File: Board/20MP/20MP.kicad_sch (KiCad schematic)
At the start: 93 parts

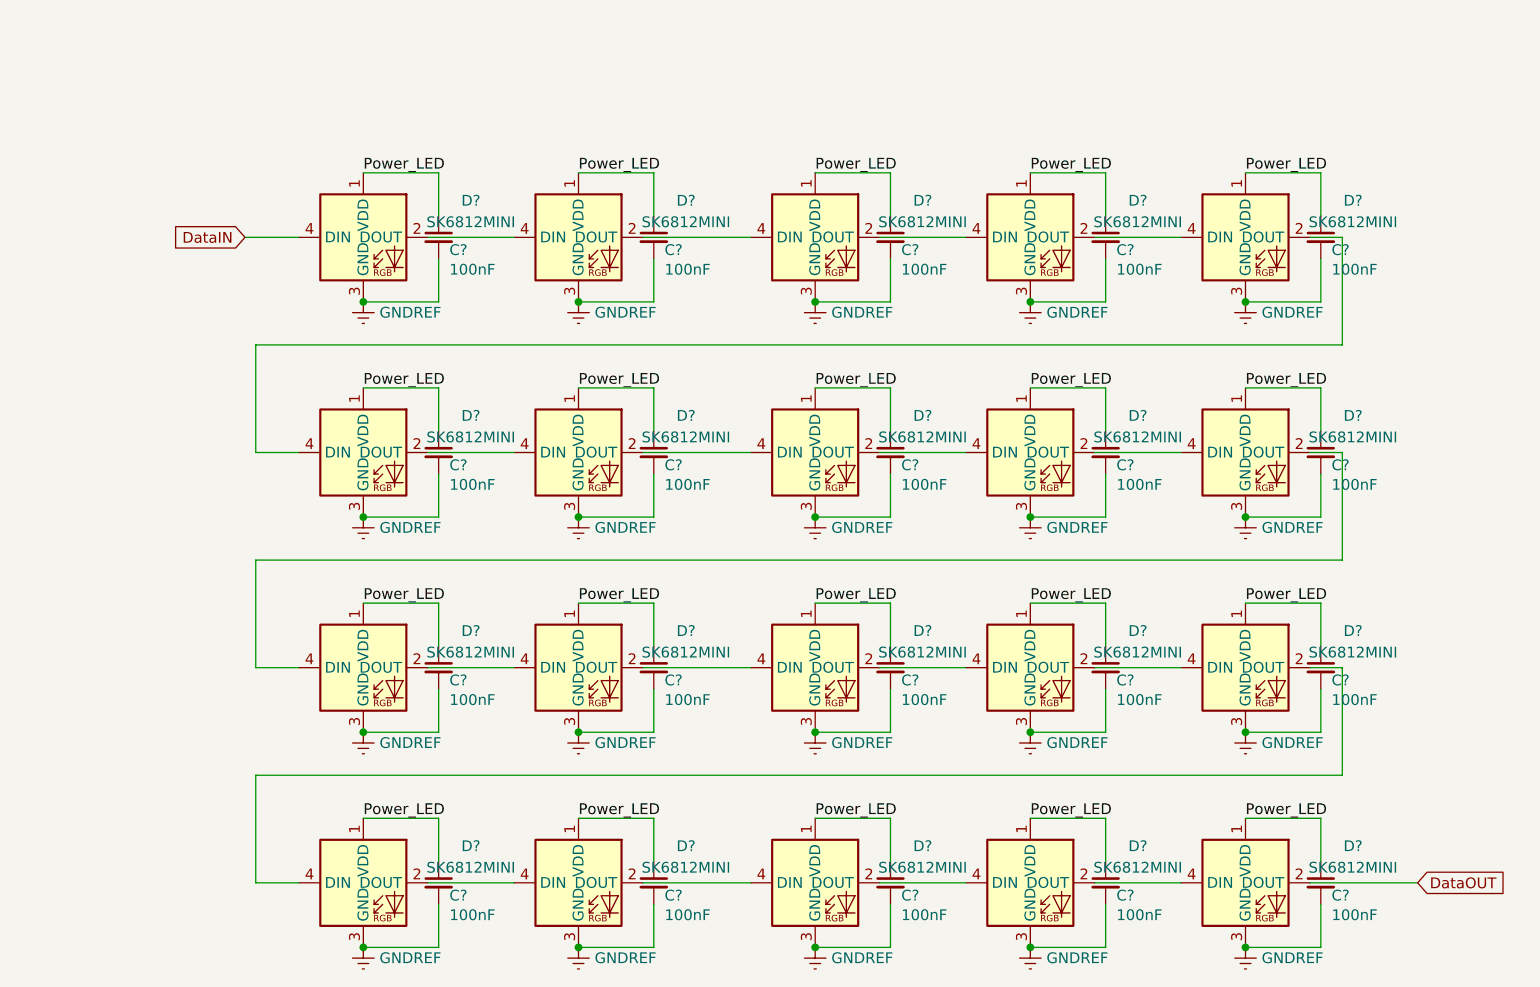
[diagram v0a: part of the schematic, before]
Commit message: removed led's
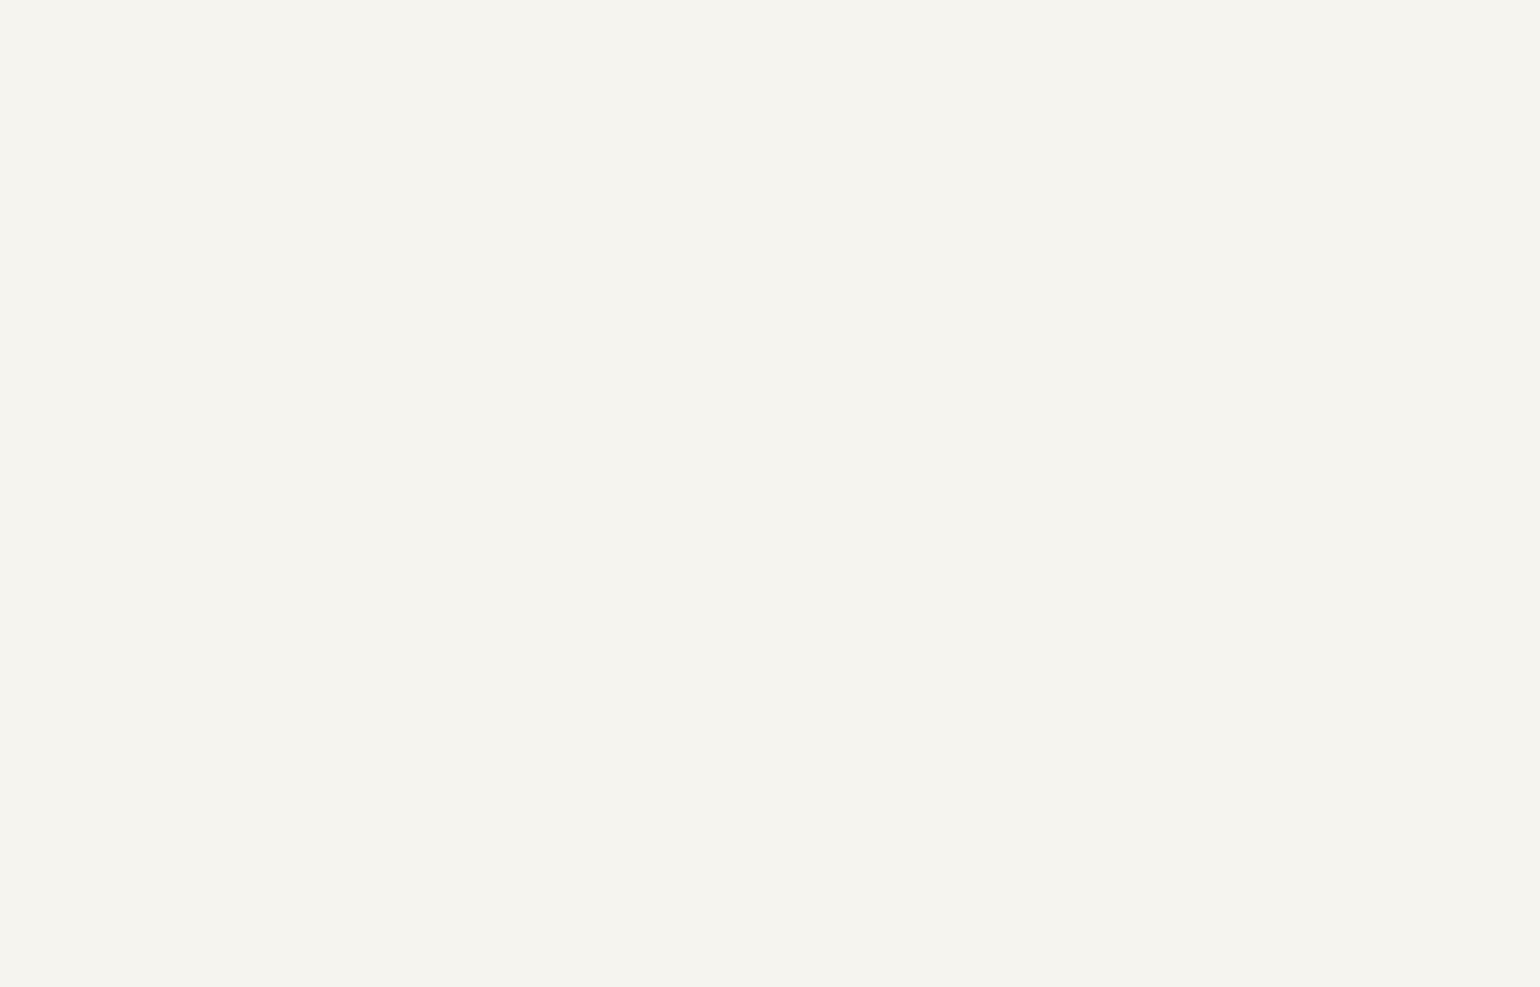
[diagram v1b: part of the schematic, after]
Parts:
- removed C? (x20): 100nF, led:led_capacitor, symbol Device:C_Small
- removed D? (x20): SK6812MINI, led:SK6812MINI_3.5x3.7mm_SMD-Flipped-Back, symbol randomSymbols:SK6812MINI-E

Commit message: removed LED's and added first librarys
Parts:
- removed D? (x22): 1.25V@150mA, led:D_SOD-123, symbol led:D_Small
- added J1: Conn_01x02_Male, Connector_JST:JST_EH_S2B-EH_1x02_P2.50mm_Horizontal, symbol Connector:Conn_01x02_Male
- added SW1: SHOU_HAN_MSK12C02-HB, led:SHOU HAN MSK12C02-HB, symbol randomSymbols:SHOU_HAN_MSK12C02-HB
- added U1: nice_nano, nice-nano-all-pins:nice_nano, symbol nice_nano:nice_nano
- MX1, MX10, MX11, MX12, MX13, MX14, MX15, MX16, MX17, MX18, MX19, MX2, MX20, MX3, MX4, MX5, MX6, MX7, MX8, MX9: renamed from MX?; footprint kailh-switches-hotswap:Kailh-Hotswap-1U -> mx-switches:CherryMX-1.00U
- gave numbers to parts that had none: 11
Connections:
- net COL0: now also U1.19 (AIN5/P0.29)
- net COL1: now also U1.18 (AIN0/P0.02)
- net COL2: now also U1.17 (P1.15)
- net COL3: now also U1.16 (P1.13)
- net COL4: now also U1.15 (P1.11)
- net COL5: now also U1.14 (NFC2/P0.10)
- net GND: now also SW1.4 (GND), U1.23 (GND), U1.3 (GND), U1.4 (GND)
- net ROW0: now also MX1.2 (ROW), MX13.2 (ROW), MX17.2 (ROW), MX5.2 (ROW), MX9.2 (ROW), SW2.S1, U1.1 (TX0/P0.06)
- net ROW1: now also MX10.2 (ROW), MX14.2 (ROW), MX18.2 (ROW), MX2.2 (ROW), MX6.2 (ROW), SW3.S1, U1.2 (RX1/P0.08)
- net ROW2: now also MX11.2 (ROW), MX15.2 (ROW), MX19.2 (ROW), MX3.2 (ROW), MX7.2 (ROW), U1.5 (P0.17)
- net ROW3: now also MX12.2 (ROW), MX16.2 (ROW), MX20.2 (ROW), MX4.2 (ROW), MX8.2 (ROW), U1.6 (P0.20)
- new net: J1.2 (Pin_2), SW1.3
- new net B+: SW1.2, U1.34 (BATIN/P0.04)
- new net B-: J1.1 (Pin_1), U1.30 (GND)
- new net VCC: U1.21 (VCC)
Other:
- moved on the sheet: MX1, MX10, MX11, MX12, MX13, MX14, MX15, MX16, MX17, MX18, MX19, MX2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

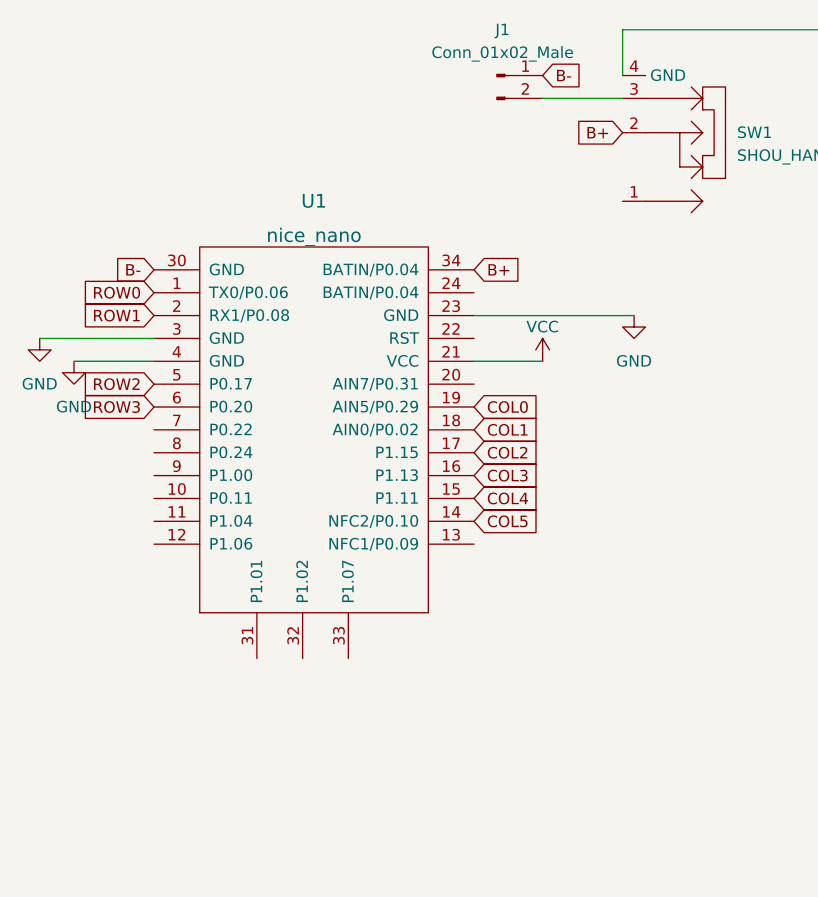
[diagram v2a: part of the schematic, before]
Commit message: added nice_nanoV2
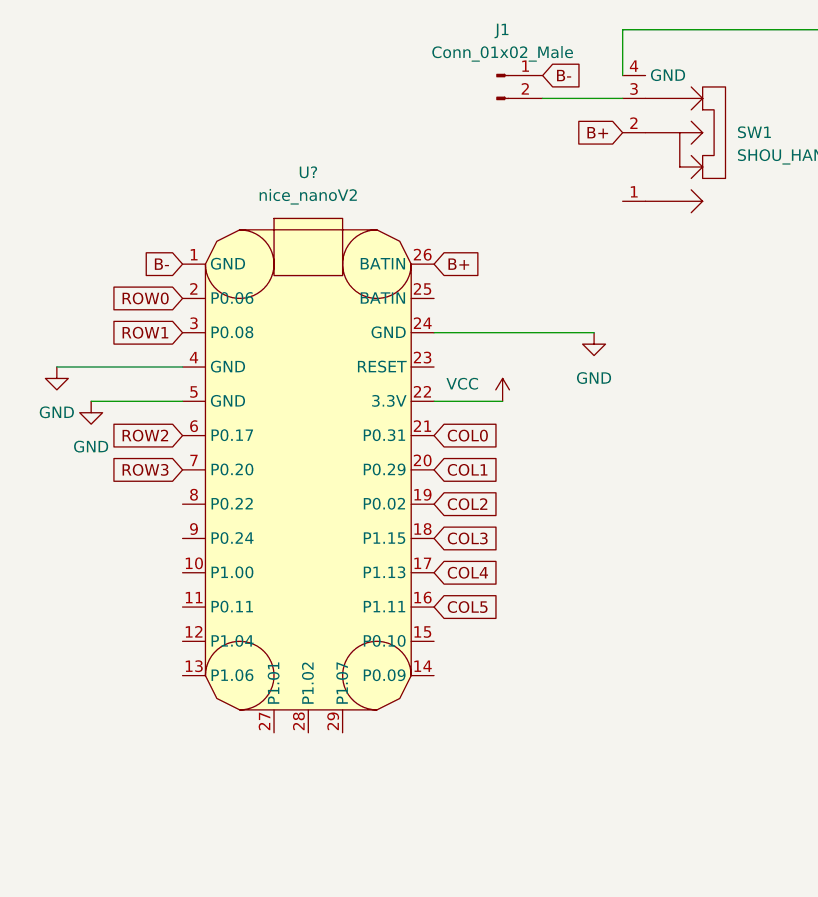
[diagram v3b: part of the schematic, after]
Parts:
- removed U1: nice_nano, nice-nano-all-pins:nice_nano, symbol nice_nano:nice_nano
- added U?: nice_nanoV2, symbol microcontroller:nice_nanoV2
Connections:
- net B+: now also U?.26 (BATIN)
- net B-: now also U?.1 (GND)
- net COL0: now also U?.21 (P0.31)
- net COL1: now also U?.20 (P0.29)
- net COL2: now also U?.19 (P0.02)
- net COL3: now also U?.18 (P1.15)
- net COL4: now also U?.17 (P1.13)
- net COL5: now also U?.16 (P1.11)
- net GND: now also U?.24 (GND), U?.4 (GND), U?.5 (GND)
- net ROW0: now also U?.2 (P0.06)
- net ROW1: now also U?.3 (P0.08)
- net ROW2: now also U?.6 (P0.17)
- net ROW3: now also U?.7 (P0.20)
- net VCC: now also U?.22 (3.3V)

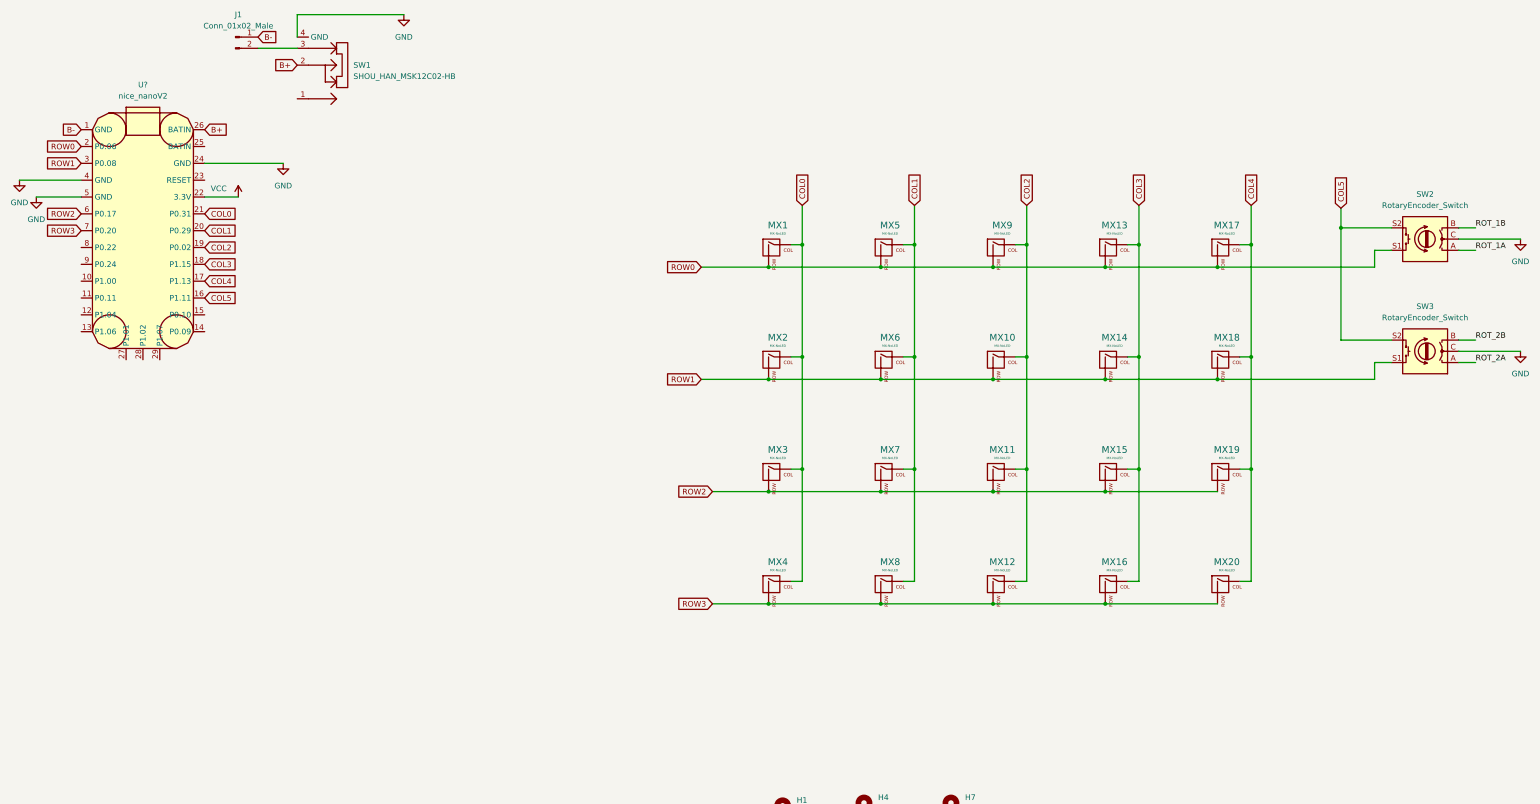
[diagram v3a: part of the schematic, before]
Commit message: PCB basic layout
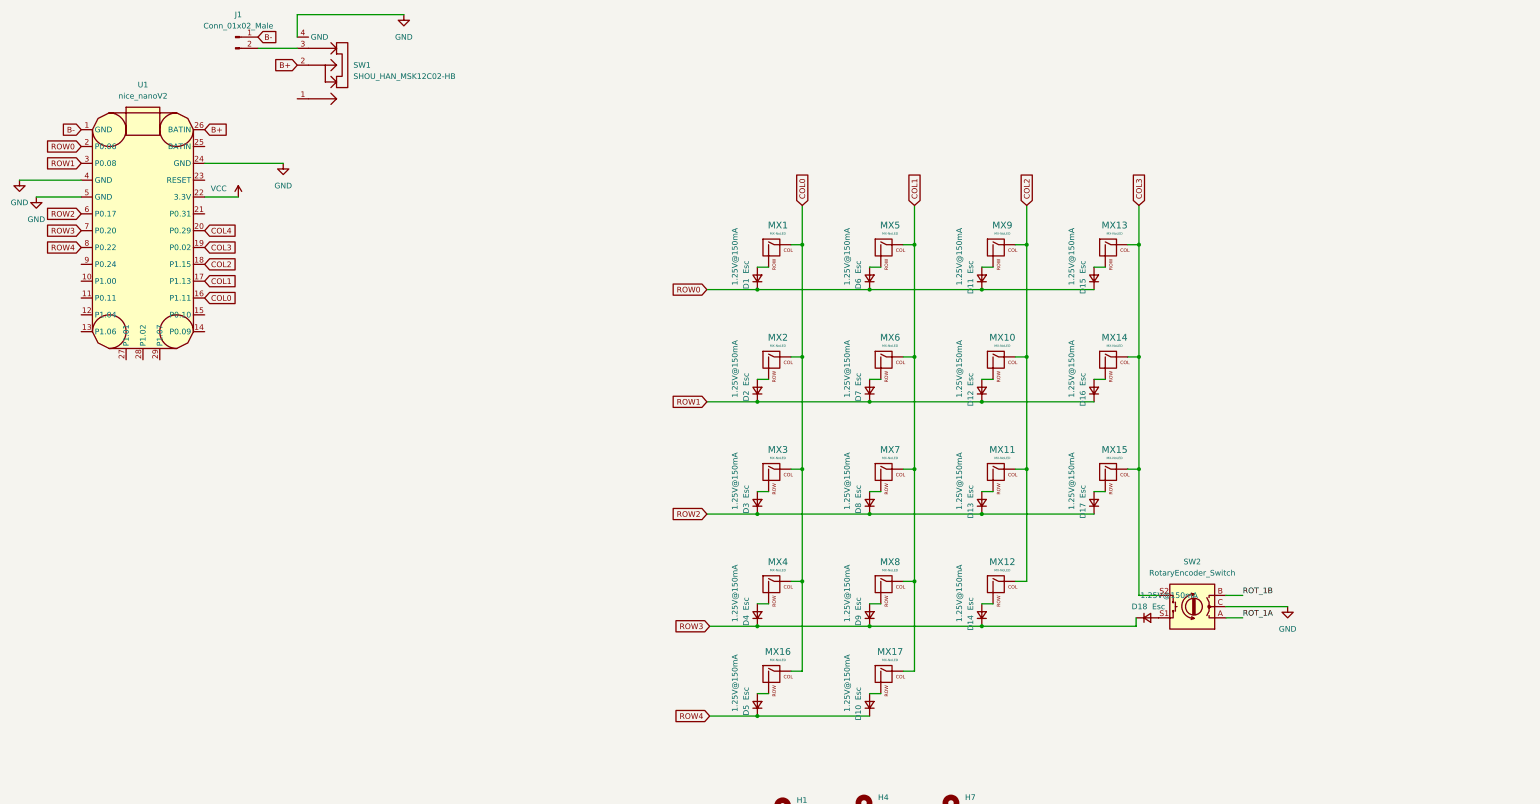
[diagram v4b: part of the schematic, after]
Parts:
- removed MX18, MX19, MX20: MX-NoLED, mx-switches:CherryMX-1.00U, symbol pcb-rescue:MX-NoLED-MX_Alps_Hybrid
- removed SW3: RotaryEncoder_Switch, led:RotaryEncoder_EC11E-Switch, symbol Device:RotaryEncoder_Switch
- added D1, D10, D11, D12, D13, D14, D15, D16, D17, D18, D2, D3, D4, D5, D6, D7, D8, D9: 1.25V@150mA, Diode_THT:D_DO-35_SOD27_P7.62mm_Horizontal, symbol led:D_Small
- J1: footprint Connector_JST:JST_EH_S2B-EH_1x02_P2.50mm_Horizontal -> led:THT_Battery
- MX14, MX15: footprint mx-switches:CherryMX-1.00U -> mx-switches:CherryMX-2.00U_90deg
- MX16: footprint mx-switches:CherryMX-1.00U -> mx-switches:CherryMX-2.00U
- U1: renamed from U?; footprint (none) -> microcontroller:nice_nanoV2
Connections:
- net COL0: now also MX16.1 (COL), U1.16 (P1.11); no longer U1.21 (P0.31)
- net COL1: now also MX17.1 (COL), U1.17 (P1.13); no longer U1.20 (P0.29)
- net COL2: now also U1.18 (P1.15); no longer U1.19 (P0.02)
- net COL3: now also SW2.S2, U1.19 (P0.02); no longer MX16.1 (COL), U1.18 (P1.15)
- net COL4: now also U1.20 (P0.29); no longer MX17.1 (COL), U1.17 (P1.13)
- net ROW0: now also D1.1 (K), D11.1 (K), D15.1 (K), D6.1 (K); no longer MX1.2 (ROW), MX13.2 (ROW), MX17.2 (ROW), MX5.2 (ROW), MX9.2 (ROW), SW2.S1
- net ROW1: now also D12.1 (K), D16.1 (K), D2.1 (K), D7.1 (K); no longer MX10.2 (ROW), MX14.2 (ROW), MX2.2 (ROW), MX6.2 (ROW)
- net ROW2: now also D13.1 (K), D17.1 (K), D3.1 (K), D8.1 (K); no longer MX11.2 (ROW), MX15.2 (ROW), MX3.2 (ROW), MX7.2 (ROW)
- net ROW3: now also D14.1 (K), D18.1 (K), D4.1 (K), D9.1 (K); no longer MX12.2 (ROW), MX16.2 (ROW), MX4.2 (ROW), MX8.2 (ROW)
- net ROW4: now reaches U1.8 (P0.22)
- net ROW4: now also D10.1 (K), D5.1 (K)
- removed net COL5: SW2.S2, U1.16 (P1.11)
- new net: D5.2 (A), MX16.2 (ROW)
- new net: D13.2 (A), MX11.2 (ROW)
- new net: D4.2 (A), MX4.2 (ROW)
- new net: D12.2 (A), MX10.2 (ROW)
- new net: D9.2 (A), MX8.2 (ROW)
- new net: D18.2 (A), SW2.S1
- new net: D7.2 (A), MX6.2 (ROW)
- new net: D17.2 (A), MX15.2 (ROW)
- new net: D14.2 (A), MX12.2 (ROW)
- new net: D15.2 (A), MX13.2 (ROW)
- new net: D3.2 (A), MX3.2 (ROW)
- new net: D8.2 (A), MX7.2 (ROW)
- new net: D1.2 (A), MX1.2 (ROW)
- new net: D11.2 (A), MX9.2 (ROW)
- new net: D16.2 (A), MX14.2 (ROW)
- new net: D2.2 (A), MX2.2 (ROW)
- new net: D6.2 (A), MX5.2 (ROW)
- new net: D10.2 (A), MX17.2 (ROW)
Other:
- moved on the sheet: SW2
